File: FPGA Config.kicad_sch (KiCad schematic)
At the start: 38 parts, among them J1 JTAG, Q1 2N7002, SW1 RESET, SW2 PROGRAM, U1 LFE5UM5G-85F-8BG381x, U2 W25Q128JVS

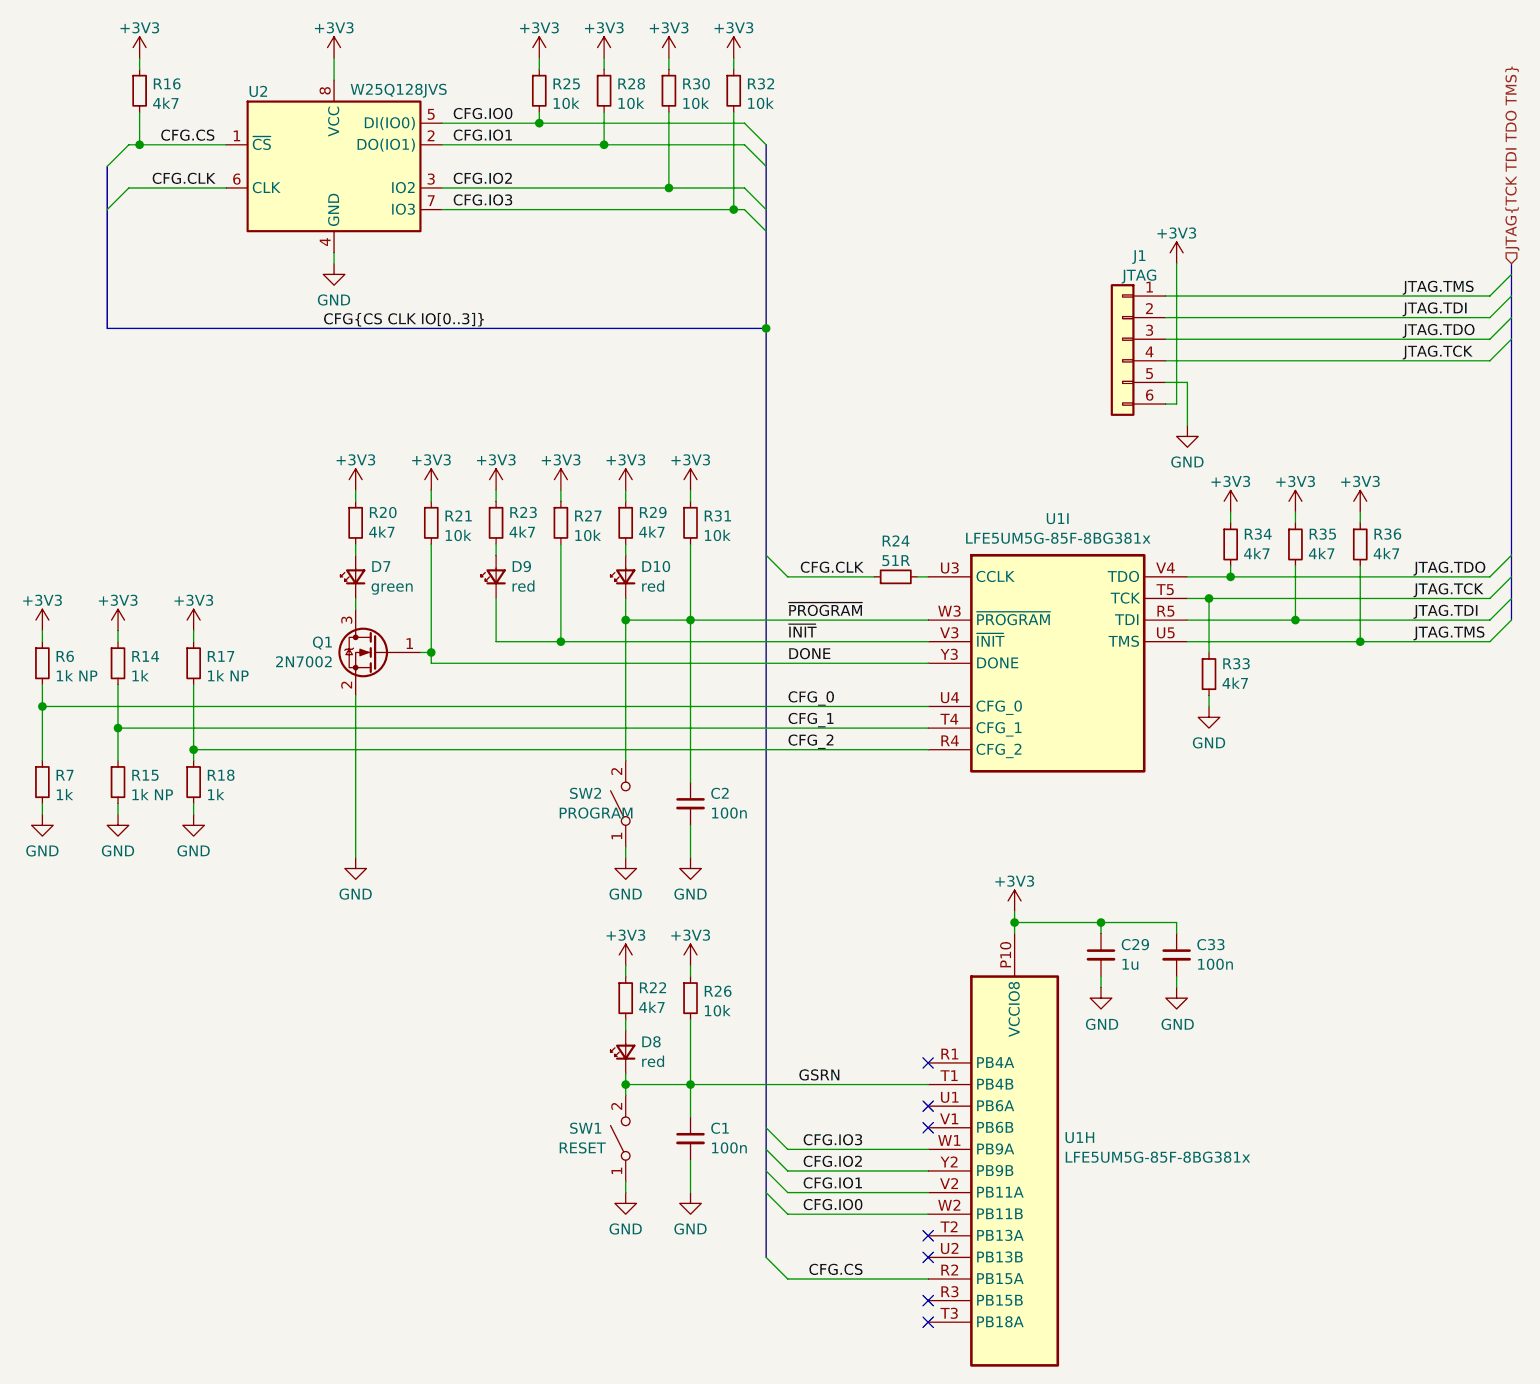
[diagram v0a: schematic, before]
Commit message: Update to KiCad 6
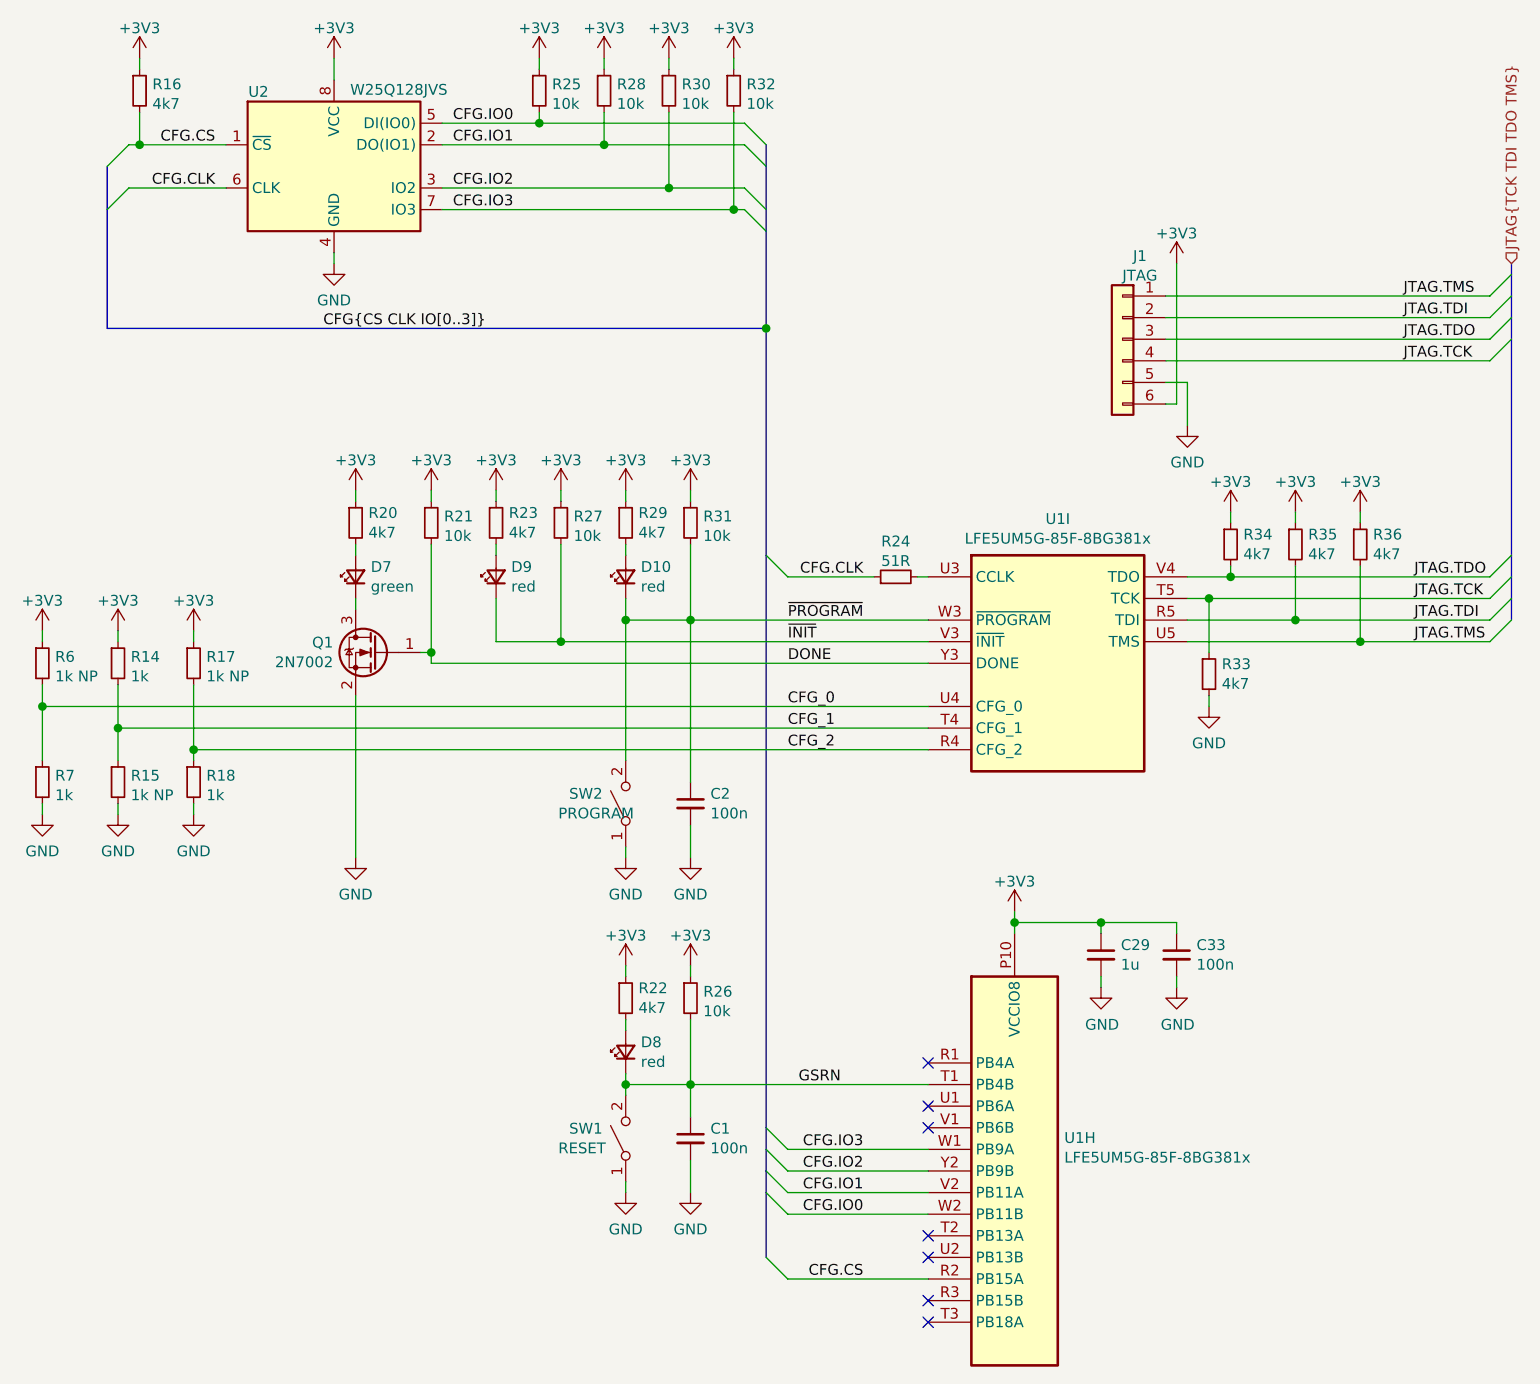
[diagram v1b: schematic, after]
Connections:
- net ~INIT renamed ~{INIT}
- net ~PROGRAM renamed ~{PROGRAM}
